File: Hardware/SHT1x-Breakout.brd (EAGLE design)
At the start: 19.1 x 19.1 mm, 9 parts, among them U1 SHT1XSMD

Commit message: Initial Revision Commit
Testing to make sure changes only happen to V_1.4 branch. Initial
layout of new revision.
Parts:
- removed R2: 10K, SparkFun:0603-RES
- removed U$1: LOGO-SFENEW, SparkFun:SFE-NEW-WEBLOGO
- removed U$2, U$3: FIDUCIAL1X2, SparkFun:FIDUCIAL-1X2
- added FID1, FID2: FIDUCIAL1X2, SparkFun-Aesthetics:FIDUCIAL-1X2
- added FRAME1: (no value), SparkFun-Aesthetics:CREATIVE_COMMONS
- added LOGO1: OSHW-LOGOS, SparkFun-Aesthetics:OSHW-LOGO-S
- added LOGO4: SFE_LOGO_FLAME.1_INCH, SparkFun-Aesthetics:SFE_LOGO_FLAME_.1
- added SJ1: JUMPER-PAD-2-NC_BY_TRACE, SparkFun-Passives:PAD-JUMPER-2-NC_BY_TRACE_YES_SILK
- added STANDOFF1, STANDOFF2: STAND-OFF, SparkFun-Electromechanical:STAND-OFF
- C1: device SparkFun:0603-CAP -> SparkFun-Capacitors:0603-CAP
- R1: device SparkFun:0603-RES -> SparkFun-Resistors:0603-RES
- U1: device SparkFun:SHT1X -> SparkFun-Sensors:SHT1X
- moved JP1 15.9 mm to (1.27, 5.08), turned to 90 degrees
- moved R1 9.96 mm to (7.62, 10.2), turned to 0 degrees
- moved U1 9.17 mm to (14.0, 8.89), turned to 0 degrees
- moved C1 5.85 mm to (5.08, 11.4), turned to 90 degrees
- moved U$4 1.80 mm to (17.8, -10.2)
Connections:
- removed net VDD: C1.2, JP1.1, R1.2, U1.4
- new net N$1: R1.1, SJ1.1
- new net VCC: C1.1, JP1.3, R1.2, U1.4
- net DATA: now also SJ1.2; no longer R1.1
- net GND: now also C1.2; no longer C1.1, R2.2
- net SCK: now also JP1.1; no longer JP1.3, R2.1
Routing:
- net GND: track 24.1 -> 0.00 mm
- net DATA: track 15.9 -> 0.00 mm, vias 1 -> 0
- net VDD: track 13.8 -> 0.00 mm
- net SCK: track 11.0 -> 0.00 mm
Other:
- board size 19.1 x 19.1 mm -> 19.1 x 17.8 mm
- board text removed: "R1"
- board text removed: "R2"

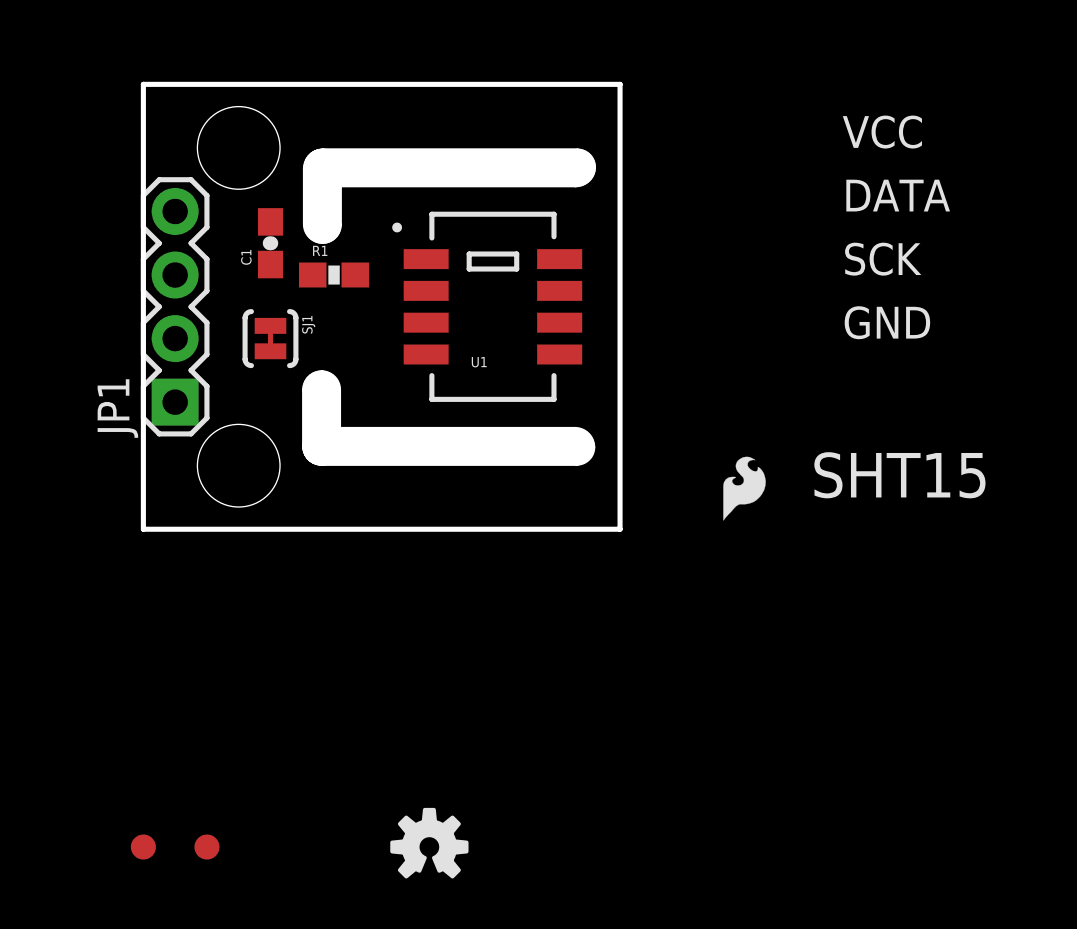
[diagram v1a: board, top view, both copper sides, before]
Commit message: Initial Layout finished
Initial Layout finished - ready for monday review
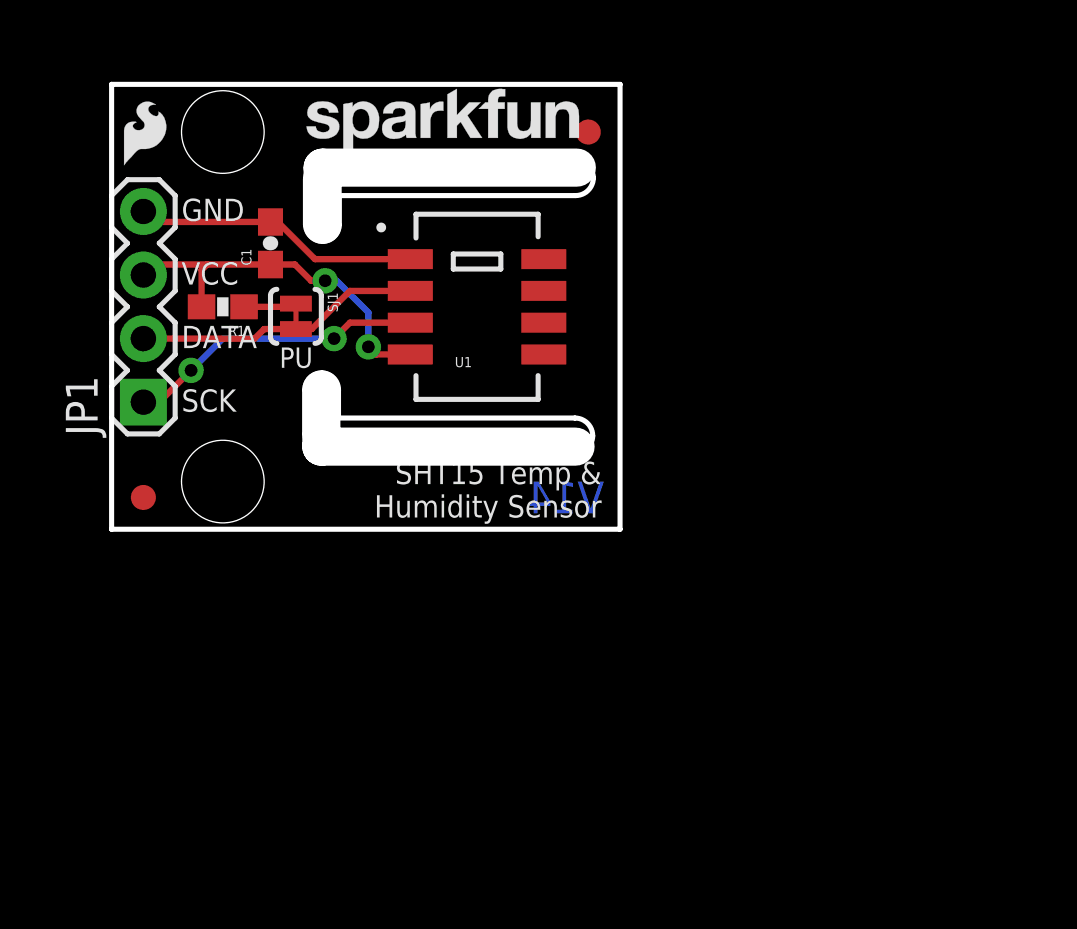
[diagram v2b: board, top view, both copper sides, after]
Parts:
- added LOGO2: SFE_LOGO_NAME.1_INCH, SparkFun-Aesthetics:SFE_LOGO_NAME_.1
- added LOGO5: SFE_LOGO_NAME_FLAME.1_INCH, SparkFun-Aesthetics:SFE_LOGO_NAME_FLAME_.1
- moved FID1 32.4 mm to (17.8, 15.9)
- moved LOGO1 28.8 mm to (12.4, 16.1), flipped to the bottom
- moved LOGO4 27.8 mm to (-1.09, 14.2)
- moved FID2 14.0 mm to (0.00, 1.27)
- moved R1 4.62 mm to (3.17, 8.89), turned to 180 degrees
- moved SJ1 1.35 mm to (6.10, 8.51)
- moved JP1 1.27 mm to (0.00, 5.08)
- moved STANDOFF2 0.90 mm to (3.17, 1.91)
- moved STANDOFF1 0.90 mm to (3.17, 15.9)
- moved U1 0.63 mm to (13.3, 8.89)
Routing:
- net VCC: track 0.00 -> 14.9 mm, vias 0 -> 2
- net SCK: track 0.00 -> 12.0 mm, vias 0 -> 2
- net GND: track 0.00 -> 11.5 mm
- net DATA: track 0.00 -> 11.5 mm
- net N$1: track 0.00 -> 2.12 mm
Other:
- board size 19.1 x 17.8 mm -> 20.3 x 17.8 mm
- board text added: "Original SHT15 size"
- board text added: "PU"
- board text added: "SHT15 Temp & Humidity Sensor"
- board text added: "V14"
- board text removed: "SHT15"

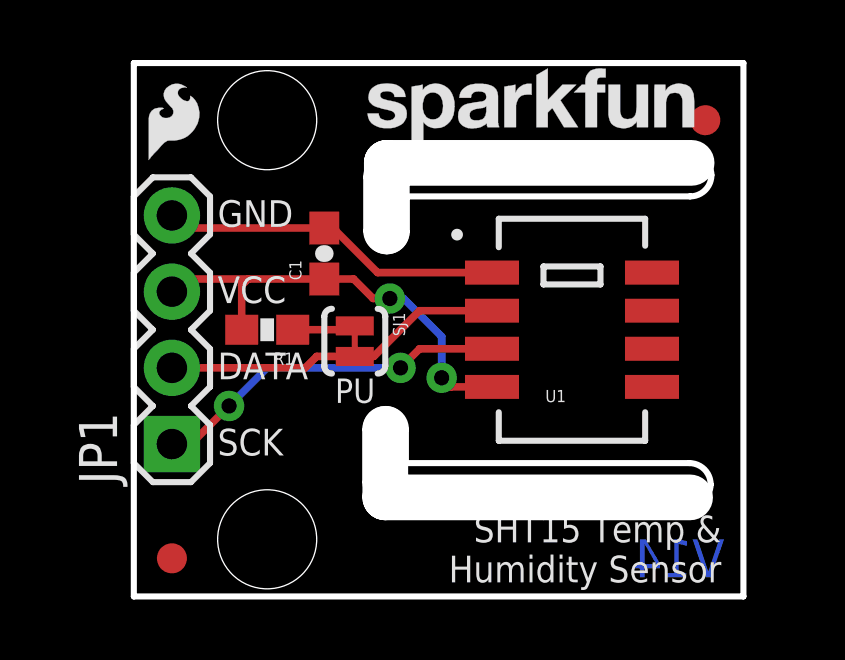
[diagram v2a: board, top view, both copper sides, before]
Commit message: Monday Review Complete
Monday Review Changes implemented. Bottom silk on pins, names and
version numbers, + a few minor fixes.
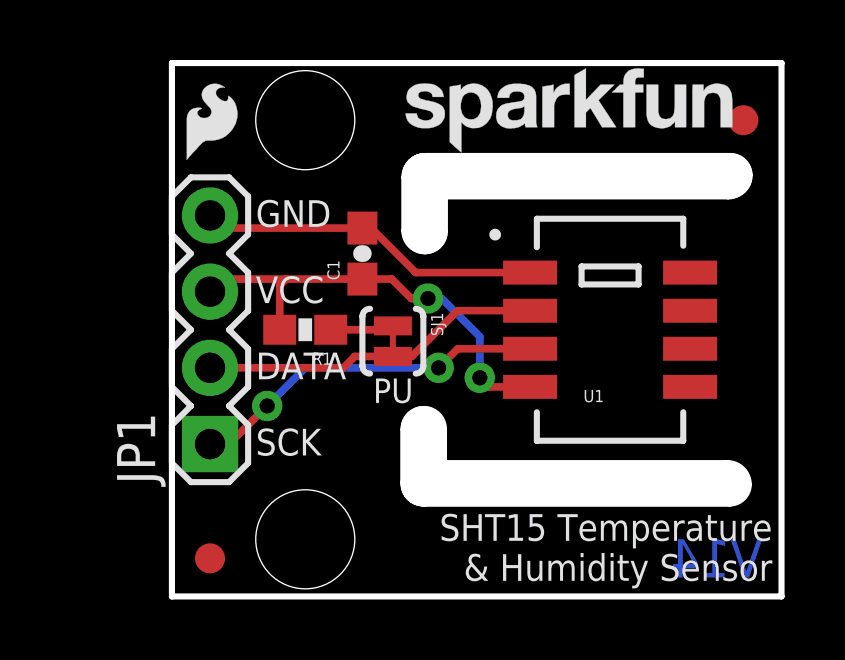
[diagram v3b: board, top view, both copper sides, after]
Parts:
- removed U$4: CREATIVE_COMMONS, SparkFun:CREATIVE_COMMONS
- SJ1: value JUMPER-PAD-2-NC_BY_TRACE -> JUMPER
- moved FRAME1 34.5 mm to (-17.8, -10.2)
- moved LOGO1 14.7 mm to (14.0, 1.40)
- moved LOGO5 1.69 mm to (20.4, 7.37)
- moved R1 1.27 mm to (4.45, 8.89)
- moved STANDOFF1 1.27 mm to (4.45, 15.9)
- moved STANDOFF2 1.27 mm to (4.45, 1.91)
- moved FID2 1.27 mm to (1.27, 1.27)
- moved JP1 1.27 mm to (1.27, 5.08)
- moved LOGO4 1.27 mm to (0.18, 14.2)
- moved C1 1.27 mm to (6.35, 11.4)
- moved FID1 1.27 mm to (19.1, 15.9)
- moved LOGO2 1.27 mm to (7.29, 14.3)
- moved SJ1 1.27 mm to (7.37, 8.51)
- moved U1 1.27 mm to (14.6, 8.89)
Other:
- outline, holes or cut-outs redrawn
- board text added: "Joel Bartlett"
- board text added: "Nathan Seidle"
- board text added: "Revised By:"
- board text added: "Route Out"
- board text added: "SHT15 Temperature & Humidity Sensor"
- board text removed: "Original SHT15 size"
- board text removed: "SHT15 Temp & Humidity Sensor"

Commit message: Ready for final QC approval before protos
Addressed QC issues. Minor route changes. Added PROD_ID to SHT_15.
Altered silk name to match website name.
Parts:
- FRAME1: value (none) -> FRAME-LETTER
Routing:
- net SCK: vias 2 -> 0
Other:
- board text added: "Humidity & Temp Sensor - SHT15"
- board text removed: "SHT15 Temperature & Humidity Sensor"
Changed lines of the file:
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@@
 <setting verticaltext="up"/>
 </settings>
-<grid distance="0.025" unitdist="inch" unit="inch" style="lines" multiple="1" display="yes" altdistance="0.025" altunitdist="inch" altunit="inch"/>
+<grid distance="0.05" unitdist="inch" unit="inch" style="lines" multiple="1" display="yes" altdistance="0.005" altunitdist="inch" altunit="inch"/>
 <layers>
 <layer number="1" name="Top" color="4" fill="1" visible="yes" active="yes"/>
@@
 <layer number="45" name="Holes" color="7" fill="1" visible="yes" active="yes"/>
 <layer number="46" name="Milling" color="3" fill="1" visible="no" active="yes"/>
-<layer number="47" name="Measures" color="7" fill="1" visible="yes" active="yes"/>
+<layer number="47" name="Measures" color="7" fill="1" visible="no" active="yes"/>
 <layer number="48" name="Document" color="7" fill="1" visible="no" active="yes"/>
 <layer number="49" name="Reference" color="14" fill="1" visible="yes" active="yes"/>
@@
 <layer number="113" name="IDFDebug" color="7" fill="1" visible="no" active="yes"/>
 <layer number="116" name="Patch_BOT" color="9" fill="4" visible="no" active="yes"/>
+<layer number="118" name="Rect_Pads" color="7" fill="1" visible="yes" active="yes"/>
 <layer number="121" name="_tsilk" color="7" fill="1" visible="no" active="yes"/>
 <layer number="122" name="_bsilk" color="7" fill="1" visible="no" active="yes"/>
@@
 <wire x1="8.4328" y1="3.0988" x2="7.7216" y2="3.81" width="0.2032" layer="20" curve="-90"/>
 <text x="6.7056" y="6.4516" size="0.8128" layer="21" font="vector" ratio="15">PU</text>
-<text x="20.0152" y="2.7432" size="0.889" layer="21" font="vector" ratio="15" rot="R180">SHT15 Temperature
-&amp; Humidity Sensor</text>
+<text x="19.2532" y="2.7432" size="0.889" layer="21" font="vector" ratio="15" rot="R180">Humidity &amp; Temp
+Sensor - SHT15</text>
 <text x="19.685" y="0.635" size="1.27" layer="16" font="vector" ratio="15" rot="MR0">V14</text>
 <text x="5.0546" y="12.319" size="0.889" layer="22" font="vector" ratio="15" rot="MR0">GND</text>
@@
 <text x="-5.08" y="-12.7" size="1.778" layer="51" font="vector" ratio="10">Revised By:</text>
 <text x="12.7" y="-10.16" size="1.778" layer="51" font="vector" ratio="9">Nathan Seidle</text>
-<text x="9.5758" y="3.302" size="1.016" layer="49" font="vector" ratio="12">Route Out</text>
-<text x="9.8044" y="13.5128" size="1.016" layer="49" font="vector" ratio="12">Route Out</text>
-<text x="5.4102" y="17.399" size="0.889" layer="22" font="vector" ratio="15" rot="MR180">SHT15 Temperature
-&amp; Humidity Sensor</text>
+<text x="9.5758" y="3.302" size="1.016" layer="51" font="vector" ratio="12">Route Out</text>
+<text x="9.8044" y="13.5128" size="1.016" layer="51" font="vector" ratio="12">Route Out</text>
 <dimension x1="0" y1="17.78" x2="20.32" y2="17.78" x3="10.16" y3="24.13" textsize="1.016" textratio="12" layer="47" unit="inch"/>
 <dimension x1="0" y1="17.78" x2="0" y2="0" x3="-7.62" y3="8.89" textsize="1.016" textratio="12" layer="47" unit="inch"/>
 <dimension x1="4.445" y1="15.875" x2="4.445" y2="1.905" x3="-3.81" y3="8.89" textsize="1.016" textratio="12" layer="47" unit="inch"/>
 <dimension x1="0" y1="17.78" x2="4.445" y2="17.78" x3="2.2225" y3="19.685" textsize="1.016" textratio="12" layer="47" unit="inch"/>
+<text x="7.5438" y="17.3482" size="0.889" layer="22" font="vector" ratio="15" rot="MR180">Humidity &amp; Temp
+Sensor - SHT15</text>
 </plain>
 <attributes>
@@
 <elements>
 <element name="JP1" library="SparkFun" package="1X04" value="" x="1.27" y="5.08" rot="R90"/>
-<element name="U1" library="SparkFun-Sensors" package="SHT1X" value="SHT1XSMD" x="14.605" y="8.89"/>
+<element name="U1" library="SparkFun-Sensors" package="SHT1X" value="SHT1XSMD" x="14.605" y="8.89">
+<attribute name="PROD_ID" value="IC-08303" x="14.605" y="8.89" size="1.778" layer="27" display="off"/>
+</element>
 <element name="C1" library="SparkFun-Capacitors" package="0603-CAP" value="0.1uF" x="6.35" y="11.43" rot="R90">
 <attribute name="PROD_ID" value="CAP-00810" x="6.35" y="11.43" size="1.778" layer="27" font="vector" ratio="15" rot="R90" display="off"/>
@@
 <element name="STANDOFF1" library="SparkFun-Electromechanical" package="STAND-OFF" value="STAND-OFF" x="4.445" y="15.875"/>
 <element name="STANDOFF2" library="SparkFun-Electromechanical" package="STAND-OFF" value="STAND-OFF" x="4.445" y="1.905"/>
-<element name="FRAME1" library="SparkFun-Aesthetics" package="CREATIVE_COMMONS" value="" x="-17.78" y="-10.16">
-<attribute name="VERSION" value="v14" x="-17.78" y="-10.16" size="1.778" layer="27" font="vector" ratio="15" display="off"/>
-<attribute name="DESIGNER" value="Joel Bartlett" x="-17.78" y="-10.16" size="1.778" layer="27" font="vector" ratio="15" display="off"/>
-</element>
+<element name="FRAME1" library="SparkFun-Aesthetics" package="CREATIVE_COMMONS" value="FRAME-LETTER" x="-17.78" y="-10.16"/>
 <element name="LOGO1" library="SparkFun-Aesthetics" package="OSHW-LOGO-S" value="OSHW-LOGOS" x="13.97" y="1.397" rot="MR0"/>
 <element name="FID1" library="SparkFun-Aesthetics" package="FIDUCIAL-1X2" value="FIDUCIAL1X2" x="19.05" y="15.875"/>
@@
 <contactref element="R1" pad="2"/>
 <wire x1="6.35" y1="10.58" x2="3.81" y2="10.58" width="0.254" layer="1"/>
-<wire x1="3.81" y1="10.58" x2="1.69" y2="10.58" width="0.254" layer="1"/>
+<wire x1="3.595" y1="10.58" x2="1.69" y2="10.58" width="0.254" layer="1"/>
 <wire x1="1.69" y1="10.58" x2="1.27" y2="10.16" width="0.254" layer="1"/>
 <via x="8.5344" y="9.9314" extent="1-16" drill="0.508"/>
 <wire x1="7.327" y1="10.58" x2="6.35" y2="10.58" width="0.254" layer="1"/>
-<wire x1="3.595" y1="8.89" x2="3.595" y2="10.365" width="0.254" layer="1"/>
-<wire x1="3.595" y1="10.365" x2="3.81" y2="10.58" width="0.254" layer="1"/>
 <wire x1="11.938" y1="6.985" x2="10.5664" y2="6.985" width="0.254" layer="1"/>
 <wire x1="10.5664" y1="6.985" x2="10.2616" y2="7.2898" width="0.254" layer="1"/>
@@
 <wire x1="10.2616" y1="8.6614" x2="8.9916" y2="9.9314" width="0.254" layer="16"/>
 <wire x1="8.9916" y1="9.9314" x2="8.5344" y2="9.9314" width="0.254" layer="16"/>
+<wire x1="3.595" y1="8.89" x2="3.595" y2="10.58" width="0.254" layer="1"/>
+<wire x1="3.595" y1="10.58" x2="3.81" y2="10.58" width="0.254" layer="1"/>
 </signal>
 <signal name="SCK">
 <contactref element="U1" pad="3"/>
 <contactref element="JP1" pad="1"/>
-<via x="3.175" y="6.35" extent="1-16" drill="0.508"/>
-<via x="8.89" y="7.62" extent="1-16" drill="0.508"/>
 <wire x1="9.525" y1="8.255" x2="11.938" y2="8.255" width="0.254" layer="1"/>
-<wire x1="9.525" y1="8.255" x2="8.89" y2="7.62" width="0.254" layer="1"/>
-<wire x1="8.89" y1="7.62" x2="4.445" y2="7.62" width="0.254" layer="16"/>
-<wire x1="4.445" y1="7.62" x2="3.175" y2="6.35" width="0.254" layer="16"/>
 <wire x1="1.27" y1="5.08" x2="1.905" y2="5.08" width="0.254" layer="1"/>
-<wire x1="1.905" y1="5.08" x2="3.175" y2="6.35" width="0.254" layer="1"/>
+<wire x1="1.905" y1="5.08" x2="3.683" y2="6.858" width="0.254" layer="1"/>
+<wire x1="3.683" y1="6.858" x2="8.128" y2="6.858" width="0.254" layer="1"/>
+<wire x1="8.128" y1="6.858" x2="9.525" y2="8.255" width="0.254" layer="1"/>
 </signal>
 <signal name="DATA">

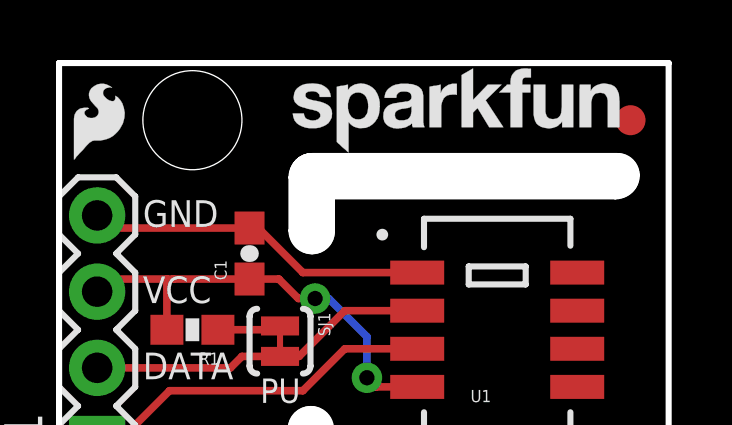
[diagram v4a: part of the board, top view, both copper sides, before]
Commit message: Moved silk to avoid fiducial
Moved silk to avoid fiducial
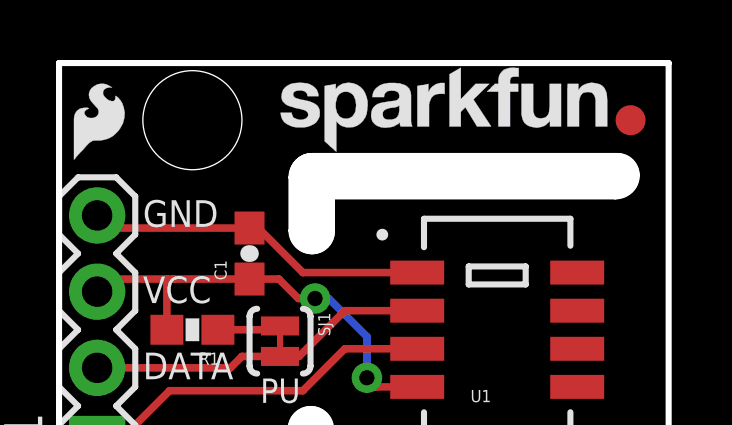
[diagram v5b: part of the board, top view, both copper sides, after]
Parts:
- moved LOGO2 0.41 mm to (6.88, 14.3)
